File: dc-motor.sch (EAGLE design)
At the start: 82 parts, among them IC1 MEGA32-A, X3 RIA_3POL, X4 RIA_3POL, X5 RIA_2POL, X6 JUMP1-4, X8 PFVERB10

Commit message: Motorstop edited
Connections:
- net N$23 renamed RÜCKMELDUNG_OUT
- removed net N$16: IC1.(AIN0/INT2)PB2, R24.1, U$38G$1.N-G1
- new net RÜCKMELDUNG_IN: IC1.(ADC3)PA3, R24.1, U$38G$1.N-G1
- net MOTORSTOP: now also IC1.(AIN0/INT2)PB2; no longer IC1.(ADC3)PA3
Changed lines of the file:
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@@
 <setting verticaltext="up"/>
 </settings>
-<grid distance="0.1" unitdist="inch" unit="inch" style="lines" multiple="1" display="no" altdistance="0.01" altunitdist="inch" altunit="inch"/>
+<grid distance="0.635" unitdist="mm" unit="mm" style="dots" multiple="1" display="yes" altdistance="0.3175" altunitdist="mm" altunit="mm"/>
 <layers>
 <layer number="1" name="Top" color="4" fill="1" visible="no" active="no"/>
@@
 </segment>
 </net>
-<net name="N$16" class="0">
-<segment>
-<pinref part="IC1" gate="G$1" pin="(AIN0/INT2)PB2"/>
-<wire x1="106.045" y1="91.44" x2="215.9" y2="91.44" width="0.1524" layer="91"/>
-<wire x1="215.9" y1="91.44" x2="217.17" y2="91.44" width="0.1524" layer="91"/>
-<wire x1="217.17" y1="91.44" x2="219.075" y2="91.44" width="0.1524" layer="91"/>
-<wire x1="219.075" y1="91.44" x2="320.04" y2="91.44" width="0.1524" layer="91"/>
-<wire x1="320.04" y1="91.44" x2="320.04" y2="85.09" width="0.1524" layer="91"/>
-<wire x1="320.04" y1="85.09" x2="320.04" y2="55.88" width="0.1524" layer="91"/>
-<pinref part="U$38" gate="G$1" pin="N-G1"/>
-<pinref part="R24" gate="G$1" pin="1"/>
-<wire x1="325.12" y1="55.88" x2="320.04" y2="55.88" width="0.1524" layer="91"/>
-<wire x1="320.04" y1="55.88" x2="320.04" y2="52.07" width="0.1524" layer="91"/>
-<junction x="320.04" y="55.88"/>
-</segment>
-</net>
-<net name="N$23" class="0">
-<segment>
-<pinref part="IC1" gate="G$1" pin="(AIN1/OC0)PB3"/>
-<wire x1="106.045" y1="93.98" x2="213.995" y2="93.98" width="0.1524" layer="91"/>
-<wire x1="213.995" y1="93.98" x2="214.63" y2="93.98" width="0.1524" layer="91"/>
-<wire x1="214.63" y1="93.98" x2="323.215" y2="93.98" width="0.1524" layer="91"/>
-<wire x1="323.215" y1="93.98" x2="323.215" y2="85.09" width="0.1524" layer="91"/>
-<wire x1="323.215" y1="85.09" x2="323.215" y2="63.5" width="0.1524" layer="91"/>
-<wire x1="323.215" y1="63.5" x2="323.215" y2="52.07" width="0.1524" layer="91"/>
-<pinref part="U$38" gate="G$2" pin="N-G1"/>
-<wire x1="338.455" y1="55.88" x2="338.455" y2="52.07" width="0.1524" layer="91"/>
-<pinref part="R28" gate="G$1" pin="1"/>
-<wire x1="338.455" y1="52.07" x2="338.455" y2="51.435" width="0.1524" layer="91"/>
-<wire x1="323.215" y1="52.07" x2="338.455" y2="52.07" width="0.1524" layer="91"/>
-<junction x="338.455" y="52.07"/>
-</segment>
-</net>
 <net name="N$59" class="0">
 <segment>
@@
 </segment>
 <segment>
-<pinref part="IC1" gate="G$1" pin="(ADC3)PA3"/>
-<wire x1="106.045" y1="116.84" x2="127.635" y2="116.84" width="0.1524" layer="91"/>
-<label x="127.635" y="116.84" size="1.778" layer="95" font="vector" xref="yes"/>
+<pinref part="IC1" gate="G$1" pin="(AIN0/INT2)PB2"/>
+<wire x1="106.045" y1="91.44" x2="133.35" y2="91.44" width="0.1524" layer="91"/>
+<label x="133.35" y="91.44" size="1.778" layer="95" font="vector" xref="yes"/>
 </segment>
 </net>
@@
 </segment>
 </net>
+<net name="RÜCKMELDUNG_IN" class="0">
+<segment>
+<pinref part="IC1" gate="G$1" pin="(ADC3)PA3"/>
+<wire x1="106.045" y1="116.84" x2="128.905" y2="116.84" width="0.1524" layer="91"/>
+<label x="128.905" y="116.84" size="1.778" layer="95" font="vector" xref="yes"/>
+</segment>
+<segment>
+<pinref part="U$38" gate="G$1" pin="N-G1"/>
+<pinref part="R24" gate="G$1" pin="1"/>
+<wire x1="325.12" y1="55.88" x2="320.04" y2="55.88" width="0.1524" layer="91"/>
+<wire x1="320.04" y1="55.88" x2="320.04" y2="52.07" width="0.1524" layer="91"/>
+<wire x1="320.04" y1="55.88" x2="315.595" y2="55.88" width="0.1524" layer="91"/>
+<junction x="320.04" y="55.88"/>
+<label x="315.595" y="55.88" size="1.778" layer="95" font="vector" rot="R180" xref="yes"/>
+</segment>
+</net>
+<net name="RÜCKMELDUNG_OUT" class="0">
+<segment>
+<pinref part="IC1" gate="G$1" pin="(AIN1/OC0)PB3"/>
+<wire x1="106.045" y1="93.98" x2="107.315" y2="93.98" width="0.1524" layer="91"/>
+<label x="107.315" y="93.98" size="1.778" layer="95" font="vector" xref="yes"/>
+</segment>
+<segment>
+<pinref part="R28" gate="G$1" pin="1"/>
+<pinref part="U$38" gate="G$2" pin="N-G1"/>
+<wire x1="338.455" y1="55.88" x2="338.455" y2="52.07" width="0.1524" layer="91"/>
+<wire x1="338.455" y1="52.07" x2="338.455" y2="51.435" width="0.1524" layer="91"/>
+<label x="326.39" y="52.07" size="1.778" layer="95" font="vector" rot="R180"/>
+<wire x1="338.455" y1="52.07" x2="346.71" y2="52.07" width="0.1524" layer="91"/>
+<junction x="338.455" y="52.07"/>
+<label x="346.71" y="52.07" size="1.778" layer="95" font="vector" xref="yes"/>
+</segment>
+</net>

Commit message: GND
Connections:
- net GND: now also IC1.(ADC0)PA0, IC1.(OC1B)PD4, IC1.PC0(SCL)
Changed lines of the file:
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@@
 <part name="R39" library="Resistor" deviceset="0805" device="" value="10k"/>
 <part name="SV1" library="con-lstb" deviceset="MA06-2" device=""/>
+<part name="U$49" library="PowerSupply" deviceset="GND" device=""/>
+<part name="U$53" library="PowerSupply" deviceset="GND" device=""/>
+<part name="U$54" library="PowerSupply" deviceset="GND" device=""/>
 </parts>
 <sheets>
@@
 </instance>
 <instance part="SV1" gate="1" x="216.535" y="260.35"/>
+<instance part="U$49" gate="G$1" x="113.03" y="50.8" rot="R90"/>
+<instance part="U$53" gate="G$1" x="113.03" y="63.5" rot="R90"/>
+<instance part="U$54" gate="G$1" x="113.03" y="109.22" rot="R90"/>
 </instances>
 <busses>
@@
 <junction x="288.29" y="194.31"/>
 </segment>
+<segment>
+<pinref part="IC1" gate="G$1" pin="(OC1B)PD4"/>
+<pinref part="U$49" gate="G$1" pin="GND"/>
+<wire x1="110.49" y1="50.8" x2="106.045" y2="50.8" width="0.1524" layer="91"/>
+</segment>
+<segment>
+<pinref part="IC1" gate="G$1" pin="PC0(SCL)"/>
+<pinref part="U$53" gate="G$1" pin="GND"/>
+<wire x1="110.49" y1="63.5" x2="106.045" y2="63.5" width="0.1524" layer="91"/>
+</segment>
+<segment>
+<pinref part="IC1" gate="G$1" pin="(ADC0)PA0"/>
+<pinref part="U$54" gate="G$1" pin="GND"/>
+<wire x1="110.49" y1="109.22" x2="106.045" y2="109.22" width="0.1524" layer="91"/>
+</segment>
 </net>

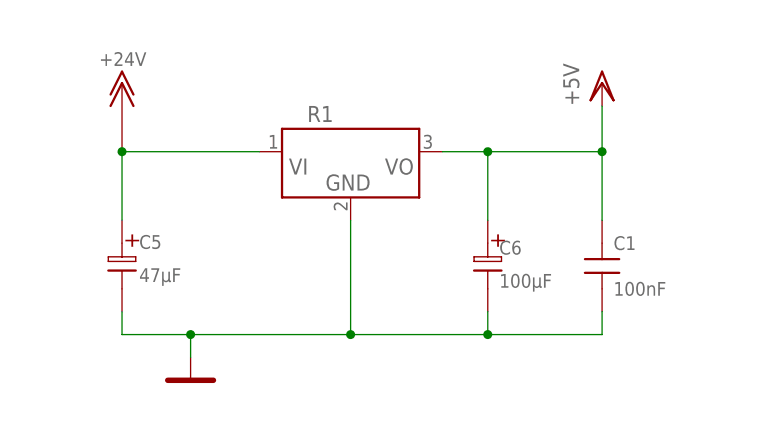
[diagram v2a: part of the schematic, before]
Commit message: DC-DC Converter value added
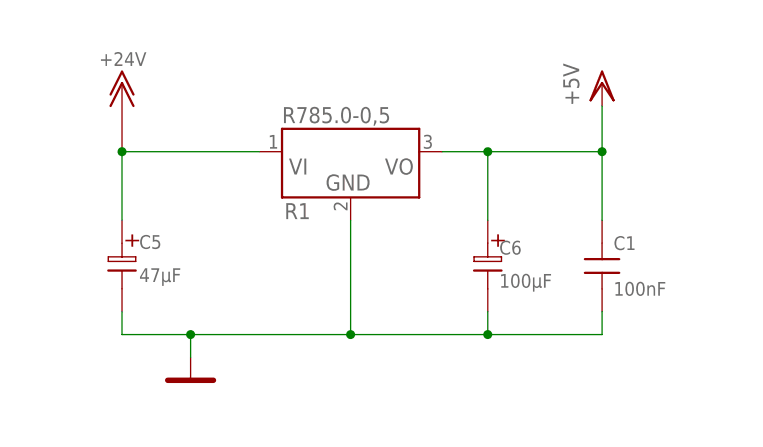
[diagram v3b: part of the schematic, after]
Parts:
- R1: value (none) -> R785.0-0,5
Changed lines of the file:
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@@
 <setting verticaltext="up"/>
 </settings>
-<grid distance="0.635" unitdist="mm" unit="mm" style="dots" multiple="1" display="yes" altdistance="0.3175" altunitdist="mm" altunit="mm"/>
+<grid distance="0.635" unitdist="mm" unit="mm" style="lines" multiple="1" display="no" altdistance="0.3175" altunitdist="mm" altunit="mm"/>
 <layers>
 <layer number="1" name="Top" color="4" fill="1" visible="no" active="no"/>
@@
 </part>
 <part name="C3" library="Capacitor" deviceset="C-BELAB" device="0805" value="100nF"/>
-<part name="R1" library="DC-DC-converter" deviceset="R-785.0-0.5" device=""/>
+<part name="R1" library="DC-DC-converter" deviceset="R-785.0-0.5" device="" value="R785.0-0,5"/>
 <part name="U$5" library="PowerSupply" deviceset="GND" device=""/>
 <part name="U$4" library="PowerSupply" deviceset="GND" device=""/>
@@
 <instance part="IC1" gate="G$1" x="85.725" y="83.82"/>
 <instance part="C3" gate="G$1" x="45.085" y="90.17" rot="R180"/>
-<instance part="R1" gate="G$1" x="43.18" y="256.54"/>
+<instance part="R1" gate="G$1" x="43.18" y="256.54" smashed="yes">
+<attribute name="NAME" x="38.735" y="262.255" size="2.032" layer="25"/>
+<attribute name="VALUE" x="38.1" y="258.445" size="2.032" layer="155"/>
+<attribute name="NAME" x="35.814" y="249.047" size="1.778" layer="95" font="vector" ratio="10"/>
+<attribute name="VALUE" x="35.56" y="259.715" size="1.778" layer="96" font="vector" ratio="10"/>
+</instance>
 <instance part="U$5" gate="G$1" x="45.085" y="77.47"/>
 <instance part="U$4" gate="G$1" x="25.4" y="231.14"/>

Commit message: RGB_LED killed
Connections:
- net RGB_GRUEN renamed LED_YELLOW
- removed net RGB_BLAU: IC1.(ICP)PD6, SV1.6
- removed net RGB_ROT: IC1.(OC2)PD7, SV1.4
- net GND: now also IC1.(ICP)PD6, IC1.(OC2)PD7
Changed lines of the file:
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@@
 <setting verticaltext="up"/>
 </settings>
-<grid distance="0.635" unitdist="mm" unit="mm" style="lines" multiple="1" display="no" altdistance="0.3175" altunitdist="mm" altunit="mm"/>
+<grid distance="0.635" unitdist="mm" unit="mm" style="dots" multiple="1" display="no" altdistance="0.01" altunitdist="inch" altunit="mm"/>
 <layers>
 <layer number="1" name="Top" color="4" fill="1" visible="no" active="no"/>
@@
 <pinref part="U$53" gate="G$1" pin="GND"/>
 <wire x1="110.49" y1="63.5" x2="106.045" y2="63.5" width="0.1524" layer="91"/>
+<wire x1="110.49" y1="63.5" x2="110.49" y2="58.42" width="0.1524" layer="91"/>
+<junction x="110.49" y="63.5"/>
+<pinref part="IC1" gate="G$1" pin="(OC2)PD7"/>
+<wire x1="110.49" y1="58.42" x2="106.045" y2="58.42" width="0.1524" layer="91"/>
+<pinref part="IC1" gate="G$1" pin="(ICP)PD6"/>
+<wire x1="106.045" y1="55.88" x2="110.49" y2="55.88" width="0.1524" layer="91"/>
+<wire x1="110.49" y1="55.88" x2="110.49" y2="58.42" width="0.1524" layer="91"/>
+<junction x="110.49" y="58.42"/>
 </segment>
 <segment>
@@
 </segment>
 </net>
-<net name="RGB_ROT" class="0">
-<segment>
-<pinref part="IC1" gate="G$1" pin="(OC2)PD7"/>
-<wire x1="106.045" y1="58.42" x2="122.555" y2="58.42" width="0.1524" layer="91"/>
-<label x="122.555" y="58.42" size="1.778" layer="95" font="vector" xref="yes"/>
-</segment>
-<segment>
-<pinref part="SV1" gate="1" pin="4"/>
-<wire x1="208.915" y1="255.27" x2="204.47" y2="255.27" width="0.1524" layer="91"/>
-<label x="204.47" y="255.27" size="1.778" layer="95" font="vector" rot="R180" xref="yes"/>
-</segment>
-</net>
-<net name="RGB_BLAU" class="0">
-<segment>
-<pinref part="IC1" gate="G$1" pin="(ICP)PD6"/>
-<wire x1="106.045" y1="55.88" x2="107.315" y2="55.88" width="0.1524" layer="91"/>
-<label x="107.315" y="55.88" size="1.778" layer="95" font="vector" xref="yes"/>
-</segment>
-<segment>
-<pinref part="SV1" gate="1" pin="6"/>
-<wire x1="208.915" y1="257.81" x2="187.96" y2="257.81" width="0.1524" layer="91"/>
-<label x="187.96" y="257.81" size="1.778" layer="95" font="vector" rot="R180" xref="yes"/>
-</segment>
-</net>
-<net name="RGB_GRUEN" class="0">
-<segment>
-<pinref part="IC1" gate="G$1" pin="(OC1A)PD5"/>
-<wire x1="106.045" y1="53.34" x2="122.555" y2="53.34" width="0.1524" layer="91"/>
-<label x="122.555" y="53.34" size="1.778" layer="95" font="vector" xref="yes"/>
-</segment>
-<segment>
-<pinref part="SV1" gate="1" pin="2"/>
-<wire x1="208.915" y1="252.73" x2="190.5" y2="252.73" width="0.1524" layer="91"/>
-<label x="190.5" y="252.73" size="1.778" layer="95" font="vector" rot="R180" xref="yes"/>
-</segment>
-</net>
 <net name="N$20" class="0">
 <segment>
@@
 </segment>
 </net>
+<net name="LED_YELLOW" class="0">
+<segment>
+<pinref part="SV1" gate="1" pin="2"/>
+<wire x1="208.915" y1="252.73" x2="190.5" y2="252.73" width="0.1524" layer="91"/>
+<label x="190.5" y="252.73" size="1.778" layer="95" font="vector" rot="R180" xref="yes"/>
+</segment>
+<segment>
+<pinref part="IC1" gate="G$1" pin="(OC1A)PD5"/>
+<wire x1="106.045" y1="53.34" x2="122.555" y2="53.34" width="0.1524" layer="91"/>
+<label x="122.555" y="53.34" size="1.778" layer="95" font="vector" xref="yes"/>
+</segment>
+</net>

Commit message: Piggyboard & Board updated
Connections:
- net LED_YELLOW renamed ERROR_LED
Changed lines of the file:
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@@
 <setting verticaltext="up"/>
 </settings>
-<grid distance="0.635" unitdist="mm" unit="mm" style="dots" multiple="1" display="no" altdistance="0.01" altunitdist="inch" altunit="mm"/>
+<grid distance="0.1" unitdist="inch" unit="inch" style="lines" multiple="1" display="no" altdistance="0.01" altunitdist="inch" altunit="inch"/>
 <layers>
 <layer number="1" name="Top" color="4" fill="1" visible="no" active="no"/>
@@
 </segment>
 </net>
-<net name="LED_YELLOW" class="0">
+<net name="ERROR_LED" class="0">
 <segment>
 <pinref part="SV1" gate="1" pin="2"/>

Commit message: Pull Down resistor added
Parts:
- added R40: 2k7, Resistor:0805
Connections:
- net GND: now also R40.1, U$3.NC
- net MOTORSTOP: now also R40.2
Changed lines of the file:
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@@
 <setting verticaltext="up"/>
 </settings>
-<grid distance="0.1" unitdist="inch" unit="inch" style="lines" multiple="1" display="no" altdistance="0.01" altunitdist="inch" altunit="inch"/>
+<grid distance="0.635" unitdist="mm" unit="mm" style="dots" multiple="1" display="yes" altdistance="0.3175" altunitdist="mm" altunit="mm"/>
 <layers>
 <layer number="1" name="Top" color="4" fill="1" visible="no" active="no"/>
@@
 <part name="U$53" library="PowerSupply" deviceset="GND" device=""/>
 <part name="U$54" library="PowerSupply" deviceset="GND" device=""/>
+<part name="R40" library="Resistor" deviceset="0805" device="" value="2k7"/>
+<part name="U$55" library="PowerSupply" deviceset="GND" device=""/>
 </parts>
 <sheets>
@@
 <instance part="U$53" gate="G$1" x="113.03" y="63.5" rot="R90"/>
 <instance part="U$54" gate="G$1" x="113.03" y="109.22" rot="R90"/>
+<instance part="R40" gate="G$1" x="161.29" y="85.725" smashed="yes" rot="R90">
+<attribute name="NAME" x="162.56" y="85.725" size="1.524" layer="95"/>
+<attribute name="VALUE" x="162.56" y="83.5025" size="1.524" layer="96"/>
+</instance>
+<instance part="U$55" gate="G$1" x="161.29" y="77.47" smashed="yes"/>
 </instances>
 <busses>
@@
 <wire x1="230.505" y1="157.48" x2="230.505" y2="165.1" width="0.1524" layer="91"/>
 <junction x="230.505" y="165.1"/>
+<pinref part="U$3" gate="G$1" pin="NC"/>
+<wire x1="248.92" y1="162.56" x2="248.92" y2="165.1" width="0.1524" layer="91"/>
+<junction x="248.92" y="165.1"/>
 </segment>
 <segment>
@@
 <pinref part="U$54" gate="G$1" pin="GND"/>
 <wire x1="110.49" y1="109.22" x2="106.045" y2="109.22" width="0.1524" layer="91"/>
+</segment>
+<segment>
+<pinref part="R40" gate="G$1" pin="1"/>
+<pinref part="U$55" gate="G$1" pin="GND"/>
+<wire x1="161.29" y1="80.645" x2="161.29" y2="80.01" width="0.1524" layer="91"/>
 </segment>
 </net>
@@
 <segment>
 <pinref part="IC1" gate="G$1" pin="(AIN0/INT2)PB2"/>
-<wire x1="106.045" y1="91.44" x2="133.35" y2="91.44" width="0.1524" layer="91"/>
-<label x="133.35" y="91.44" size="1.778" layer="95" font="vector" xref="yes"/>
-</segment>
-</net>
+<wire x1="106.045" y1="91.44" x2="161.29" y2="91.44" width="0.1524" layer="91"/>
+<label x="165.735" y="91.44" size="1.778" layer="95" font="vector" xref="yes"/>
+<pinref part="R40" gate="G$1" pin="2"/>
+<wire x1="161.29" y1="91.44" x2="165.735" y2="91.44" width="0.1524" layer="91"/>
+<wire x1="161.29" y1="91.44" x2="161.29" y2="90.805" width="0.1524" layer="91"/>
+<junction x="161.29" y="91.44"/>
+</segment>
+</net>

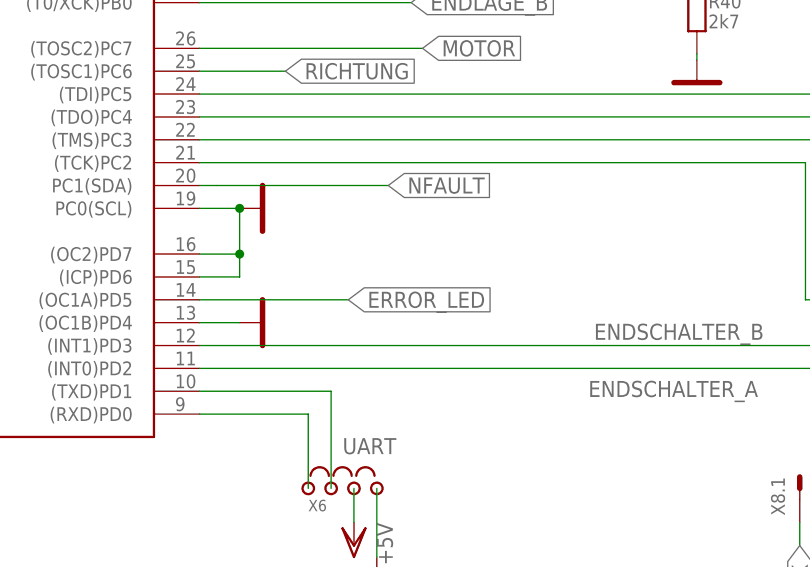
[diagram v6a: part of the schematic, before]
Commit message: PWR_LED Connected
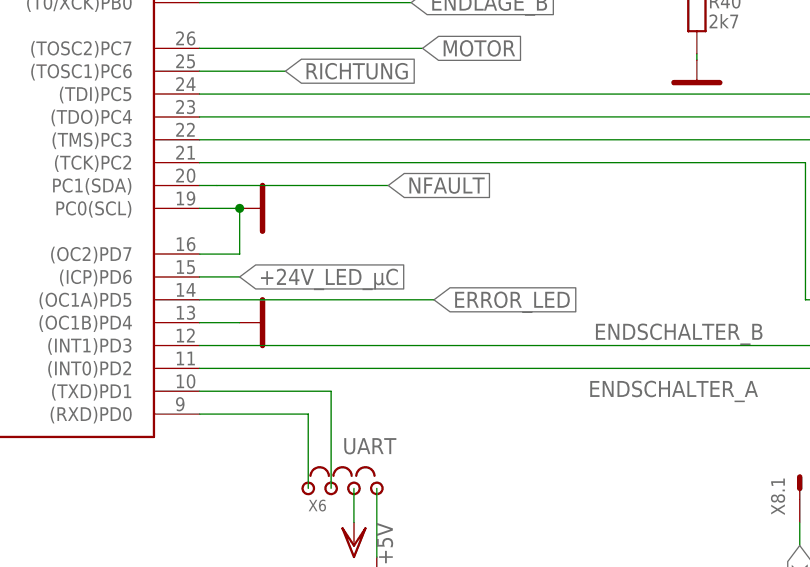
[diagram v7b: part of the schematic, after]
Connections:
- net +24V_LED_µC: now also IC1.(ICP)PD6
- net GND: no longer IC1.(ICP)PD6
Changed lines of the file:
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@@
 <setting verticaltext="up"/>
 </settings>
-<grid distance="0.635" unitdist="mm" unit="mm" style="dots" multiple="1" display="yes" altdistance="0.3175" altunitdist="mm" altunit="mm"/>
+<grid distance="0.635" unitdist="mm" unit="mm" style="lines" multiple="1" display="no" altdistance="0.01" altunitdist="inch" altunit="mm"/>
 <layers>
 <layer number="1" name="Top" color="4" fill="1" visible="no" active="no"/>
@@
 <pinref part="IC1" gate="G$1" pin="(OC2)PD7"/>
 <wire x1="110.49" y1="58.42" x2="106.045" y2="58.42" width="0.1524" layer="91"/>
-<pinref part="IC1" gate="G$1" pin="(ICP)PD6"/>
-<wire x1="106.045" y1="55.88" x2="110.49" y2="55.88" width="0.1524" layer="91"/>
-<wire x1="110.49" y1="55.88" x2="110.49" y2="58.42" width="0.1524" layer="91"/>
-<junction x="110.49" y="58.42"/>
 </segment>
 <segment>
@@
 <wire x1="208.915" y1="260.35" x2="208.28" y2="260.35" width="0.1524" layer="91"/>
 </segment>
+<segment>
+<pinref part="IC1" gate="G$1" pin="(ICP)PD6"/>
+<wire x1="106.045" y1="55.88" x2="110.49" y2="55.88" width="0.1524" layer="91"/>
+<label x="110.49" y="55.88" size="1.778" layer="95" font="vector" xref="yes"/>
+</segment>
 </net>
 <net name="N$41" class="0">
@@
 <segment>
 <pinref part="IC1" gate="G$1" pin="(OC1A)PD5"/>
-<wire x1="106.045" y1="53.34" x2="122.555" y2="53.34" width="0.1524" layer="91"/>
-<label x="122.555" y="53.34" size="1.778" layer="95" font="vector" xref="yes"/>
-</segment>
-</net>
+<wire x1="106.045" y1="53.34" x2="132.08" y2="53.34" width="0.1524" layer="91"/>
+<label x="132.08" y="53.34" size="1.778" layer="95" font="vector" xref="yes"/>
+</segment>
+</net>
